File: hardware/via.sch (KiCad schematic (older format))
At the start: 3 parts

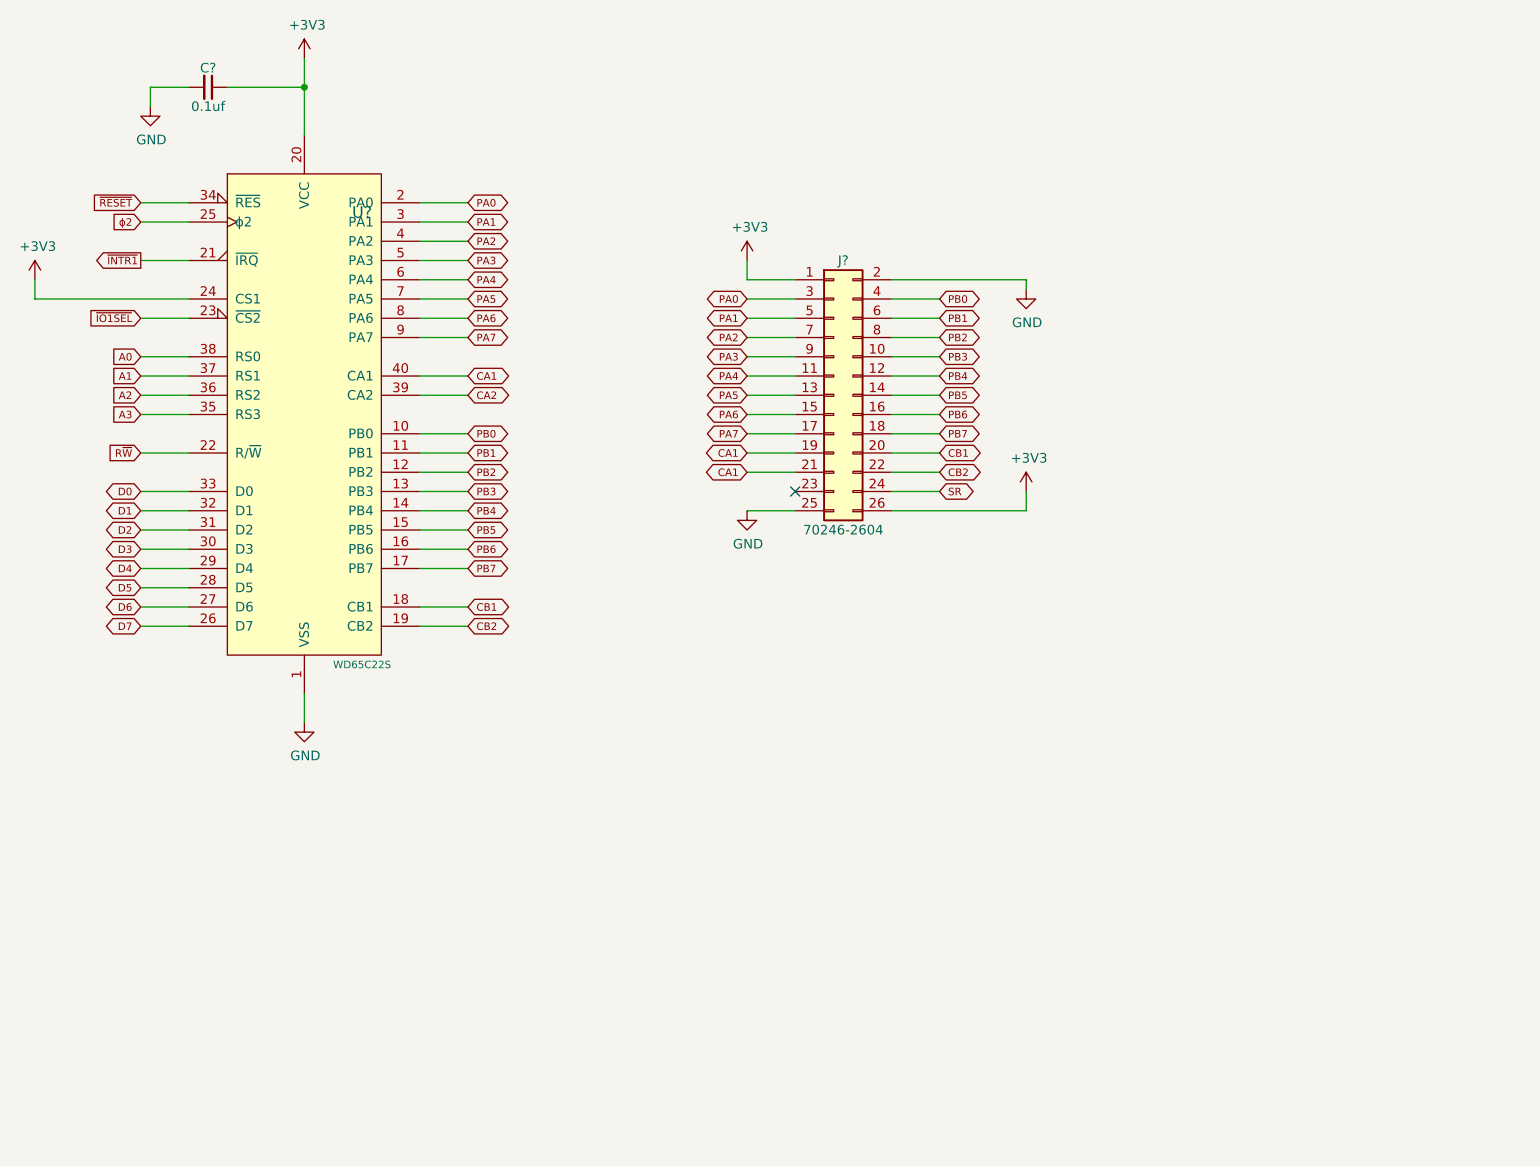
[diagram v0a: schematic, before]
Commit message: Add SPI and missing caps on MAX3232s.
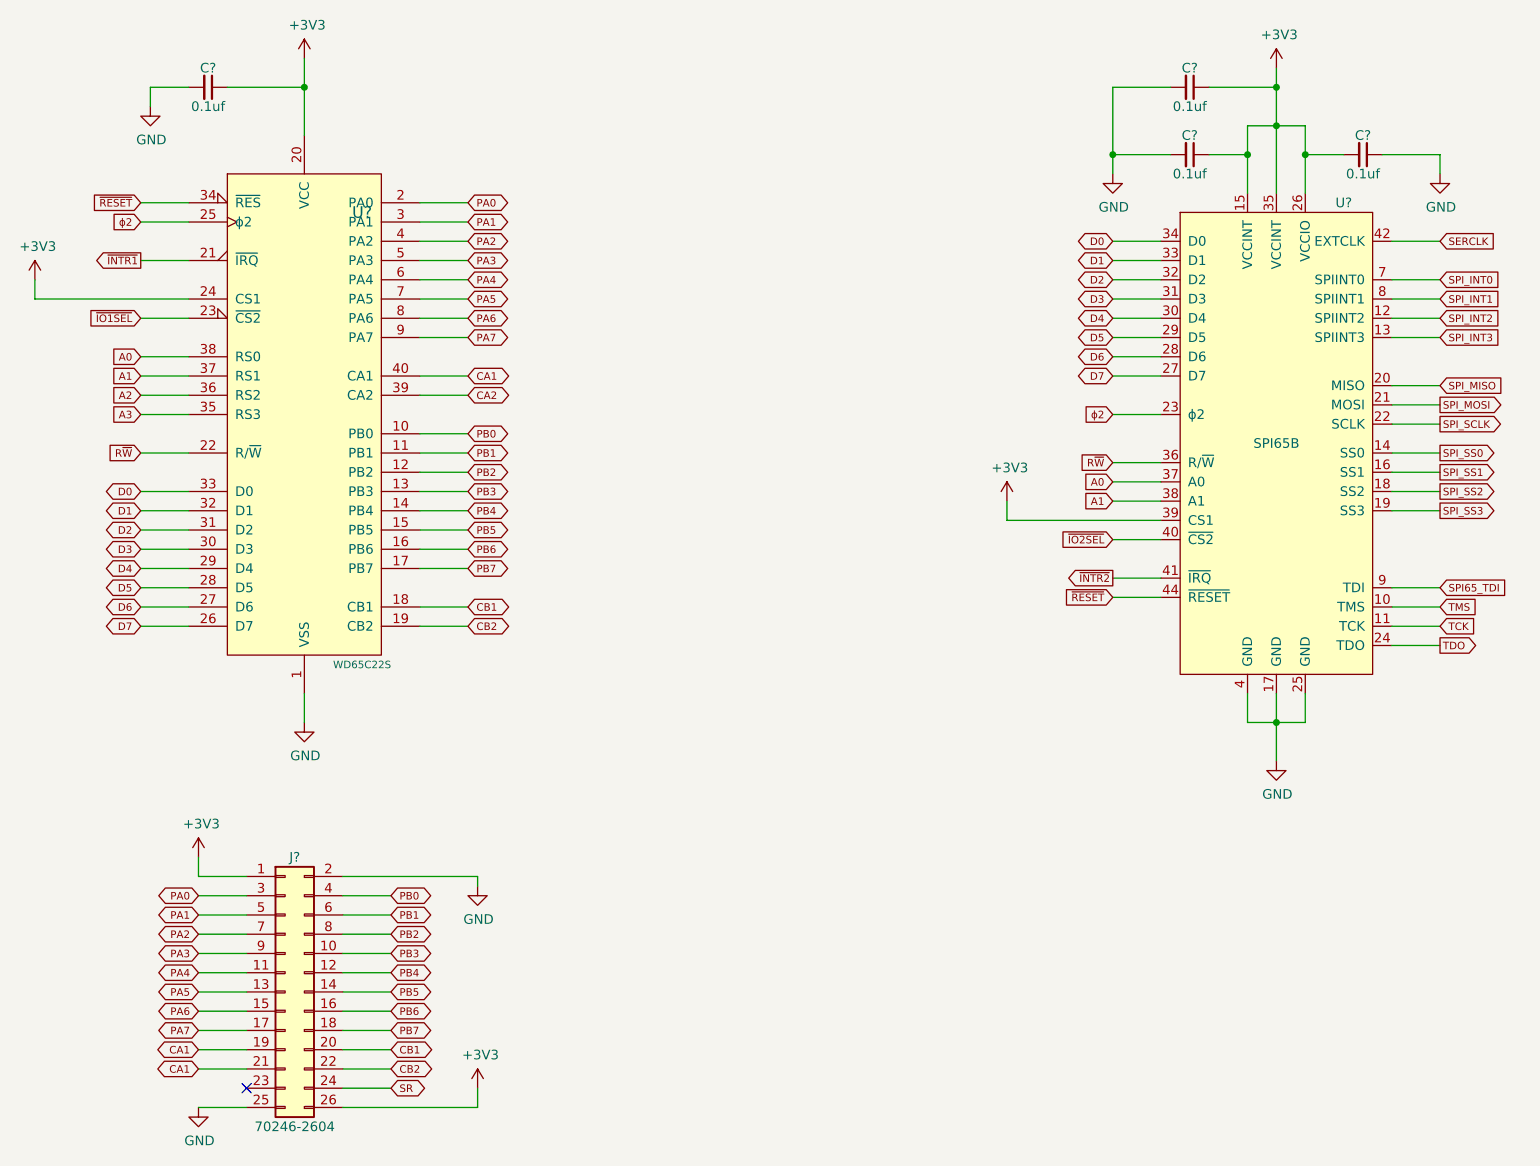
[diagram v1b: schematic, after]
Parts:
- added C? (x3): 0.1uf, symbol Device:C_Small
- added U?: SPI65B, Package_QFP:TQFP-44_10x10mm_P0.8mm, symbol custom_chips:SPI65B
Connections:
- net +3V3: now also C?.1, C?.1, C?.2, U?.15 (VCCINT), U?.26 (VCCIO), U?.35 (VCCINT), U?.39 (CS1)
- net A0: now also U?.37 (A0)
- net A1: now also U?.38 (A1)
- net D0: now also U?.34 (D0)
- net D1: now also U?.33 (D1)
- net D2: now also U?.32 (D2)
- net D3: now also U?.31 (D3)
- net D4: now also U?.30 (D4)
- net D5: now also U?.29 (D5)
- net D6: now also U?.28 (D6)
- net D7: now also U?.27 (D7)
- net GND: now also C?.1, C?.2, C?.2, U?.17 (GND), U?.25 (GND), U?.4 (GND)
- net R~W: now also U?.36 (R/~W)
- net ~RESET: now also U?.44 (~RESET)
- net ϕ2: now also U?.23 (ϕ2)
- new net SERCLK: U?.42 (EXTCLK)
- new net SPI65_TDI: U?.9 (TDI)
- new net SPI_INT0: U?.7 (SPIINT0)
- new net SPI_INT1: U?.8 (SPIINT1)
- new net SPI_INT2: U?.12 (SPIINT2)
- new net SPI_INT3: U?.13 (SPIINT3)
- new net SPI_MISO: U?.20 (MISO)
- new net SPI_MOSI: U?.21 (MOSI)
- new net SPI_SCLK: U?.22 (SCLK)
- new net SPI_SS0: U?.14 (SS0)
- new net SPI_SS1: U?.16 (SS1)
- new net SPI_SS2: U?.18 (SS2)
- new net SPI_SS3: U?.19 (SS3)
- new net TCK: U?.11 (TCK)
- new net TDO: U?.24 (TDO)
- new net TMS: U?.10 (TMS)
- new net ~INTR2: U?.41 (~IRQ)
- new net ~IO2SEL: U?.40 (~CS2)
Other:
- moved on the sheet: J?
